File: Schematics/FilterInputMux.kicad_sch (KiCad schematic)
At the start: 82 parts, among them J234 Conn_01x05, J237 Conn_01x05, J240 Conn_01x05, J243 Conn_01x05, J245 Conn_01x05, J246 Conn_01x05, J247 Conn_01x05, J255 Conn_01x05, J256 Conn_01x05, J257 Conn_01x05, J258 Conn_01x05, J259 Conn_01x05, J51 Conn_01x04, J52 Conn_01x04, J53 Conn_01x04, J76 Conn_01x04, J77 Conn_01x04, J78 Conn_01x04, J79 Conn_01x04, J80 Conn_01x04, J82 Conn_01x04, J83 Conn_01x04, J88 Conn_01x02, J89 Conn_01x02, J91 Conn_01x03, U249 PCF8574, U250 LM1117-3.3, U282 DG212C, U283 DG212C, U61 TL074, U62 TL074, U63 TL074, U64 TL074, U65 TL072

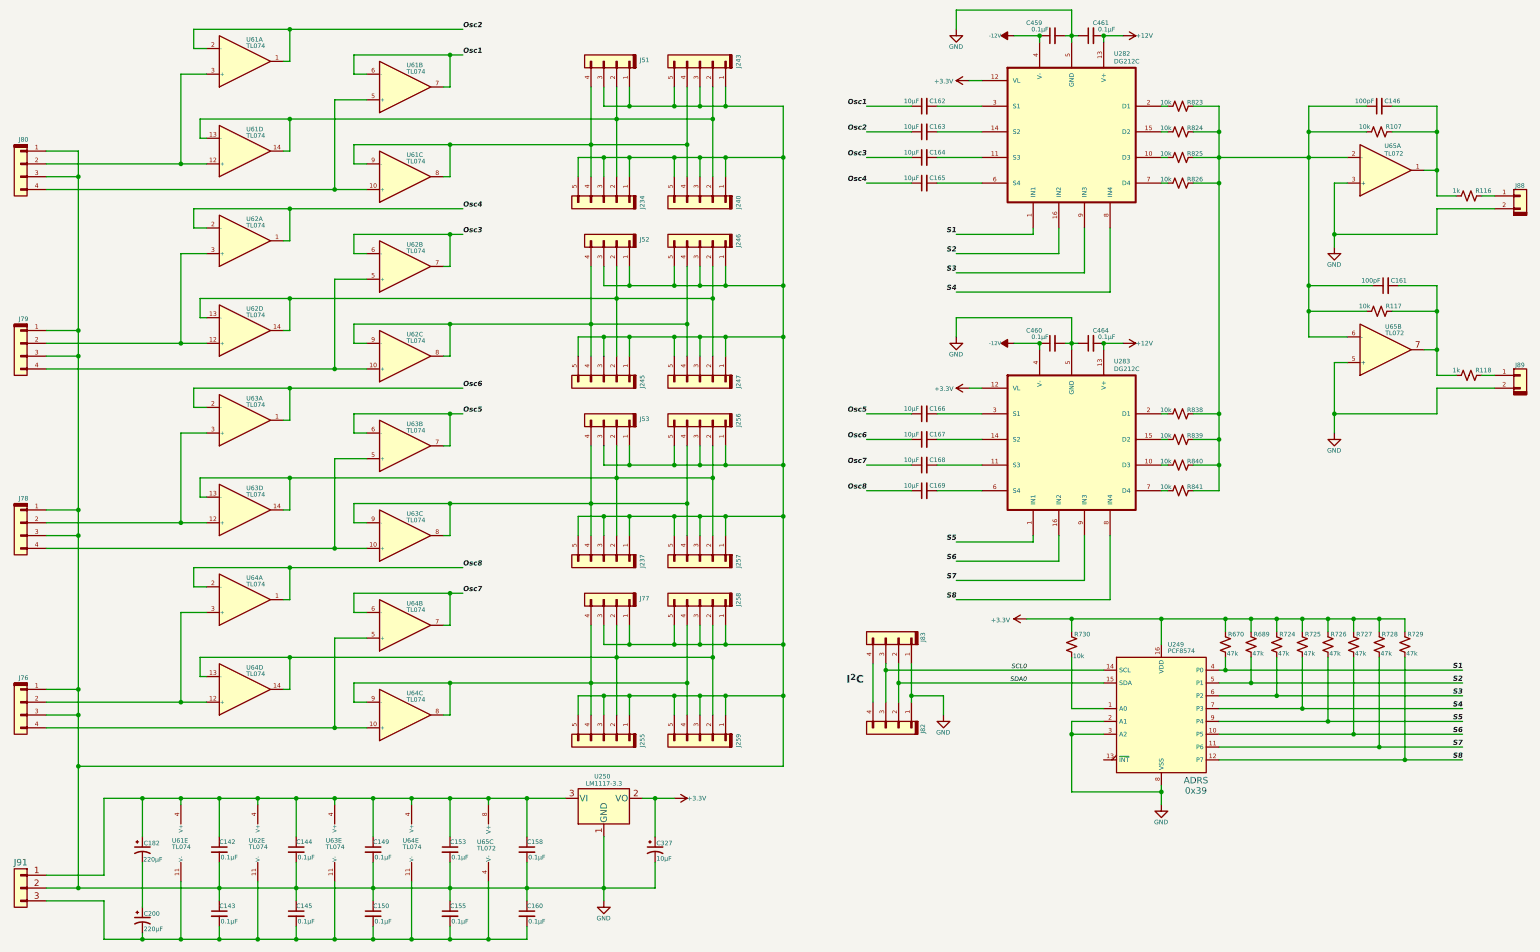
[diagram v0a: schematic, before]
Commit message: Corrected audio I/O on many schematics and added date to them.  Minor tweaks in voice interfaces.
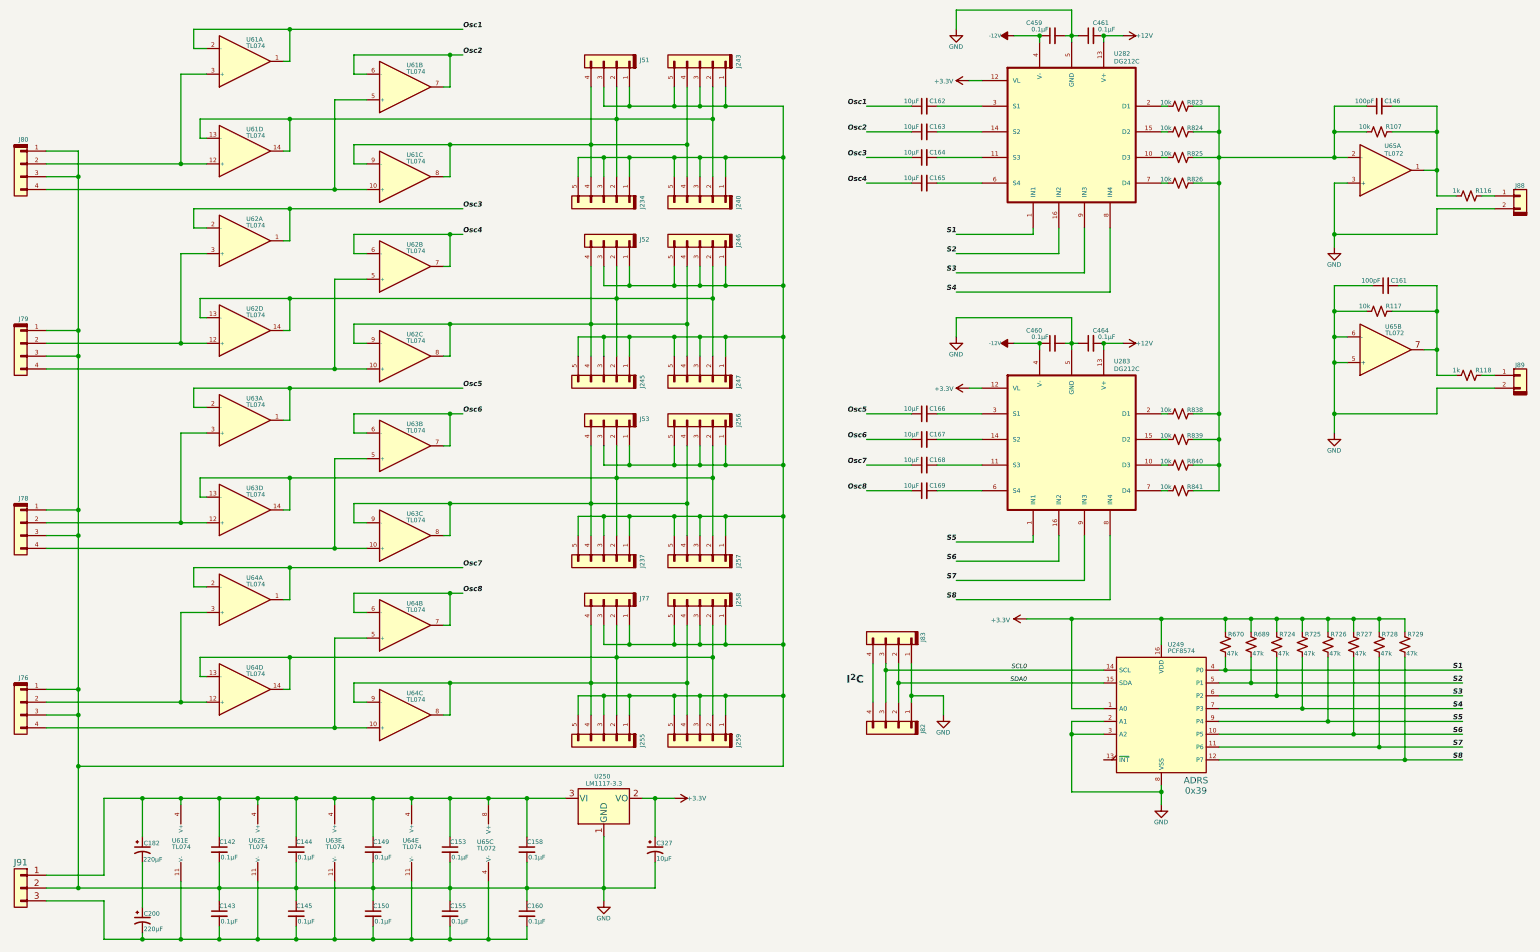
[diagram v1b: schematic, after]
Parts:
- removed R730: 10k, symbol Device:R_Small_US
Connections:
- net +3.3V: now also U249.1 (A0)
- net GND: now also C161.1, R117.1, U65.6 (-)
- net Osc1: now also U61.1, U61.2 (-); no longer U61.6 (-), U61.7
- net Osc2: now also U61.6 (-), U61.7; no longer U61.1, U61.2 (-)
- net Osc3: now also U62.1, U62.2 (-); no longer U62.6 (-), U62.7
- net Osc4: now also U62.6 (-), U62.7; no longer U62.1, U62.2 (-)
- net Osc5: now also U63.1, U63.2 (-); no longer U63.6 (-), U63.7
- net Osc6: now also U63.6 (-), U63.7; no longer U63.1, U63.2 (-)
- net Osc7: now also U64.1, U64.2 (-); no longer U64.6 (-), U64.7
- net Osc8: now also U64.6 (-), U64.7; no longer U64.1, U64.2 (-)
- net at C146.1, R107.1, R823.2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: no longer C161.1, R117.1, U65.6 (-)
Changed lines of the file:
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@@
 	(generator_version "9.0")
 	(paper "USLegal")
+	(title_block
+		(date "2025-11-28")
+	)
 	(text "I^{2}C"
 		(exclude_from_sim no)
@@
 	)
 	(junction
-		(at 271.78 74.93)
-		(diameter 0)
-		(color 0 0 0 0)
-	)
-	(junction
 		(at 254 49.53)
 		(diameter 0)
@@
 	)
 	(junction
+		(at 276.86 39.37)
+		(diameter 0)
+		(color 0 0 0 0)
+	)
+	(junction
 		(at 231.14 20.32)
 		(diameter 0)
@@
 	)
 	(junction
+		(at 276.86 44.45)
+		(diameter 0)
+		(color 0 0 0 0)
+	)
+	(junction
 		(at 101.6 113.03)
 		(diameter 0)
@@
 	)
 	(junction
+		(at 276.86 85.09)
+		(diameter 0)
+		(color 0 0 0 0)
+	)
+	(junction
 		(at 190.5 148.59)
 		(diameter 0)
@@
 	)
 	(junction
-		(at 271.78 69.85)
-		(diameter 0)
-		(color 0 0 0 0)
-	)
-	(junction
 		(at 63.5 171.45)
 		(diameter 0)
@@
 	)
 	(junction
-		(at 271.78 39.37)
-		(diameter 0)
-		(color 0 0 0 0)
-	)
-	(junction
 		(at 167.64 115.57)
 		(diameter 0)
@@
 	)
 	(junction
-		(at 271.78 44.45)
-		(diameter 0)
-		(color 0 0 0 0)
-	)
-	(junction
 		(at 78.74 157.48)
 		(diameter 0)
@@
 	)
 	(junction
+		(at 276.86 74.93)
+		(diameter 0)
+		(color 0 0 0 0)
+	)
+	(junction
 		(at 137.16 34.29)
 		(diameter 0)
@@
 	)
 	(junction
+		(at 276.86 80.01)
+		(diameter 0)
+		(color 0 0 0 0)
+	)
+	(junction
 		(at 55.88 199.39)
 		(diameter 0)
@@
 	(wire
 		(pts
-			(xy 271.78 80.01) (xy 279.4 80.01)
+			(xy 276.86 80.01) (xy 279.4 80.01)
 		)
 		(stroke
@@
 	(wire
 		(pts
-			(xy 271.78 39.37) (xy 283.21 39.37)
-		)
-		(stroke
-			(width 0)
-			(type default)
-		)
-	)
-	(wire
-		(pts
 			(xy 218.44 81.28) (xy 218.44 82.55)
 		)
@@
 	(wire
 		(pts
-			(xy 271.78 80.01) (xy 271.78 74.93)
+			(xy 276.86 80.01) (xy 276.86 74.93)
 		)
 		(stroke
@@
 	(wire
 		(pts
-			(xy 271.78 44.45) (xy 279.4 44.45)
-		)
-		(stroke
-			(width 0)
-			(type default)
-		)
-	)
-	(wire
-		(pts
 			(xy 185.42 144.78) (xy 185.42 152.4)
 		)
@@
 	(wire
 		(pts
+			(xy 276.86 74.93) (xy 283.21 74.93)
+		)
+		(stroke
+			(width 0)
+			(type default)
+		)
+	)
+	(wire
+		(pts
 			(xy 48.26 116.84) (xy 53.34 116.84)
 		)
@@
 	(wire
 		(pts
-			(xy 271.78 74.93) (xy 283.21 74.93)
-		)
-		(stroke
-			(width 0)
-			(type default)
-		)
-	)
-	(wire
-		(pts
 			(xy 213.36 81.28) (xy 218.44 81.28)
 		)
@@
 	(wire
 		(pts
-			(xy 271.78 39.37) (xy 271.78 44.45)
+			(xy 276.86 39.37) (xy 276.86 44.45)
 		)
 		(stroke
@@
 	(wire
 		(pts
-			(xy 271.78 44.45) (xy 271.78 69.85)
-		)
-		(stroke
-			(width 0)
-			(type default)
-		)
-	)
-	(wire
-		(pts
 			(xy 48.26 171.45) (xy 48.26 172.72)
 		)
@@
 	(wire
 		(pts
-			(xy 271.78 34.29) (xy 271.78 39.37)
+			(xy 276.86 34.29) (xy 276.86 39.37)
 		)
 		(stroke
@@
 	(wire
 		(pts
+			(xy 276.86 44.45) (xy 279.4 44.45)
+		)
+		(stroke
+			(width 0)
+			(type default)
+		)
+	)
+	(wire
+		(pts
 			(xy 48.26 99.06) (xy 53.34 99.06)
 		)
@@
 	(wire
 		(pts
+			(xy 276.86 39.37) (xy 283.21 39.37)
+		)
+		(stroke
+			(width 0)
+			(type default)
+		)
+	)
+	(wire
+		(pts
 			(xy 129.54 66.04) (xy 129.54 77.47)
 		)
@@
 	(wire
 		(pts
-			(xy 271.78 69.85) (xy 284.48 69.85)
+			(xy 276.86 69.85) (xy 284.48 69.85)
 		)
 		(stroke
@@
 	(wire
 		(pts
-			(xy 224.79 138.43) (xy 224.79 135.89)
-		)
-		(stroke
-			(width 0)
-			(type default)
-		)
-	)
-	(wire
-		(pts
 			(xy 198.12 39.37) (xy 207.01 39.37)
 		)
@@
 	(wire
 		(pts
+			(xy 276.86 80.01) (xy 276.86 85.09)
+		)
+		(stroke
+			(width 0)
+			(type default)
+		)
+	)
+	(wire
+		(pts
 			(xy 55.88 189.23) (xy 55.88 191.77)
 		)
@@
 	(wire
 		(pts
-			(xy 271.78 34.29) (xy 283.21 34.29)
+			(xy 276.86 34.29) (xy 283.21 34.29)
 		)
 		(stroke
@@
 	(wire
 		(pts
-			(xy 254 44.45) (xy 271.78 44.45)
+			(xy 254 44.45) (xy 276.86 44.45)
 		)
 		(stroke
@@
 	(wire
 		(pts
-			(xy 271.78 69.85) (xy 271.78 74.93)
+			(xy 276.86 69.85) (xy 276.86 74.93)
 		)
 		(stroke
@@
 	(wire
 		(pts
-			(xy 224.79 143.51) (xy 224.79 153.67)
+			(xy 224.79 135.89) (xy 224.79 153.67)
 		)
 		(stroke
@@
 	)
 	(label "Osc3"
-		(at 104.14 59.69 0)
+		(at 104.14 54.61 0)
 		(effects
 			(font
@@
 	)
 	(label "Osc4"
-		(at 104.14 54.61 0)
+		(at 104.14 59.69 0)
 		(effects
 			(font
@@
 	)
 	(label "Osc1"
-		(at 104.14 24.13 0)
+		(at 104.14 19.05 0)
 		(effects
 			(font
@@
 	)
 	(label "Osc7"
-		(at 104.14 130.81 0)
+		(at 104.14 125.73 0)
 		(effects
 			(font
@@
 	)
 	(label "Osc8"
-		(at 104.14 125.73 0)
+		(at 104.14 130.81 0)
 		(effects
 			(font
@@
 	)
 	(label "Osc2"
-		(at 104.14 19.05 0)
+		(at 104.14 24.13 0)
 		(effects
 			(font
@@
 	)
 	(label "Osc5"
-		(at 104.14 95.25 0)
+		(at 104.14 90.17 0)
 		(effects
 			(font
@@
 	)
 	(label "Osc6"
-		(at 104.14 90.17 0)
+		(at 104.14 95.25 0)
 		(effects
 			(font
@@
 					(unit 1)
 				)
-			)
-		)
-	)
-	(symbol
-		(lib_id "Device:R_Small_US")
-		(at 224.79 140.97 0)
-		(unit 1)
-		(exclude_from_sim no)
-		(in_bom yes)
-		(on_board yes)
-		(dnp no)
-		(property "Reference" "R730"
-			(at 225.298 138.938 0)
-			(effects
-				(font
-					(size 0.889 0.889)
-				)
-				(justify left)
-			)
-		)
-		(property "Value" "10k"
-			(at 225.044 143.256 0)
-			(effects
-				(font
-					(size 0.889 0.889)
-				)
-				(justify left)
-			)
-		)
-		(property "Footprint" ""
-			(at 224.79 140.97 0)
-			(effects
-				(font
-					(size 1.27 1.27)
-				)
-				(hide yes)
-			)
-		)
-		(property "Datasheet" "~"
-			(at 224.79 140.97 0)
-			(effects
-				(font
-					(size 1.27 1.27)
-				)
-				(hide yes)
-			)
-		)
-		(property "Description" ""
-			(at 224.79 140.97 0)
-			(effects
-				(font
-					(size 1.27 1.27)
-				)
-				(hide yes)
-			)
-		)
-		(pin "1"
-		)
-		(pin "2"
-		)
-		(instances
-			(project "Synth32"
-				(path "/718f017d-28fe-4e29-b548-40db8e21cec7/92fe7bea-64b6-40b3-8e51-c7dbcedff8cc/92ea8d6c-7c0a-471f-be0b-71be39e4a0a2"
-					(reference "R730")
-					(unit 1)
-				)
